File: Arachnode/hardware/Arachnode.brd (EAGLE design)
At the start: 71.1 x 33.7 mm, 37 parts, among them J1 PINHEAD-17-REV, J2 PINHEAD-17-REV, U1 BQ24210, U2 DS1337

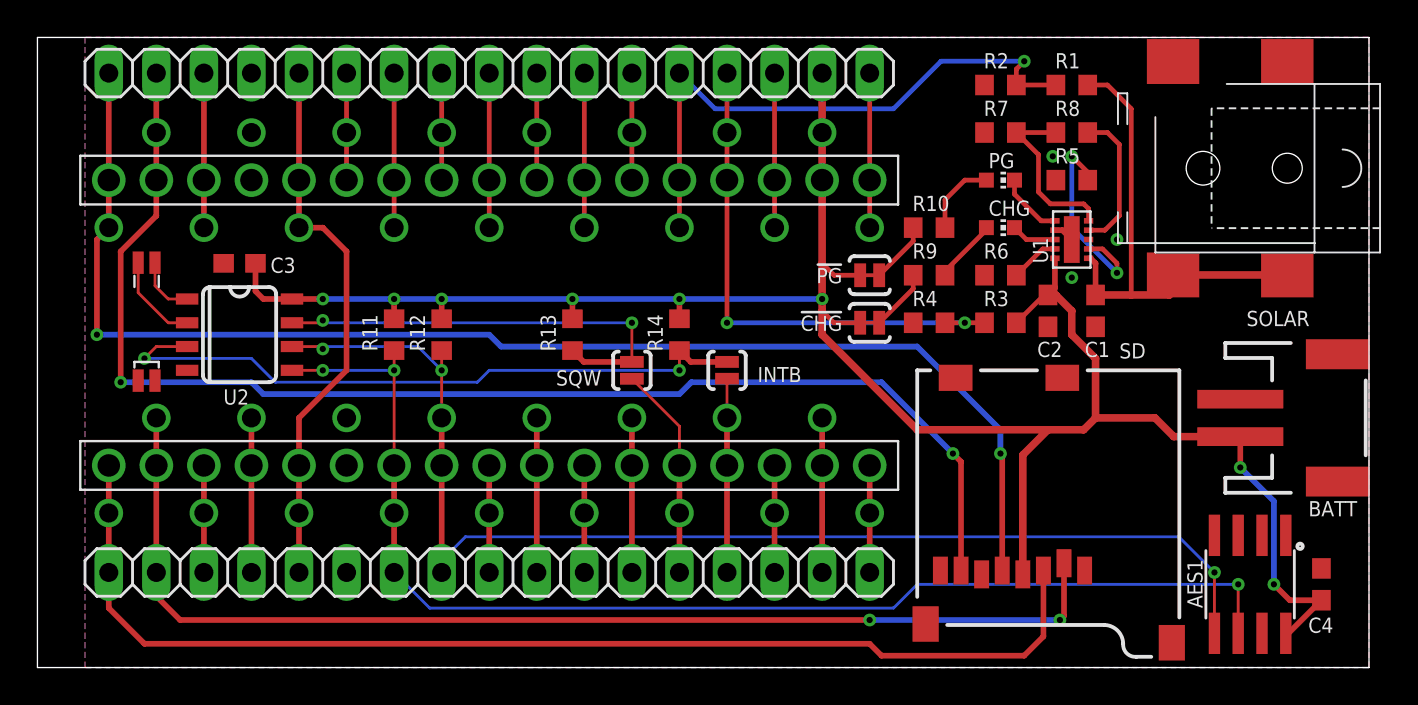
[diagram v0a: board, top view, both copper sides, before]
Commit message: -- Re-arranged Arachnode to solve connector interference. -- Created pinout diagrams for Arachnio -- Added sketch for serial console
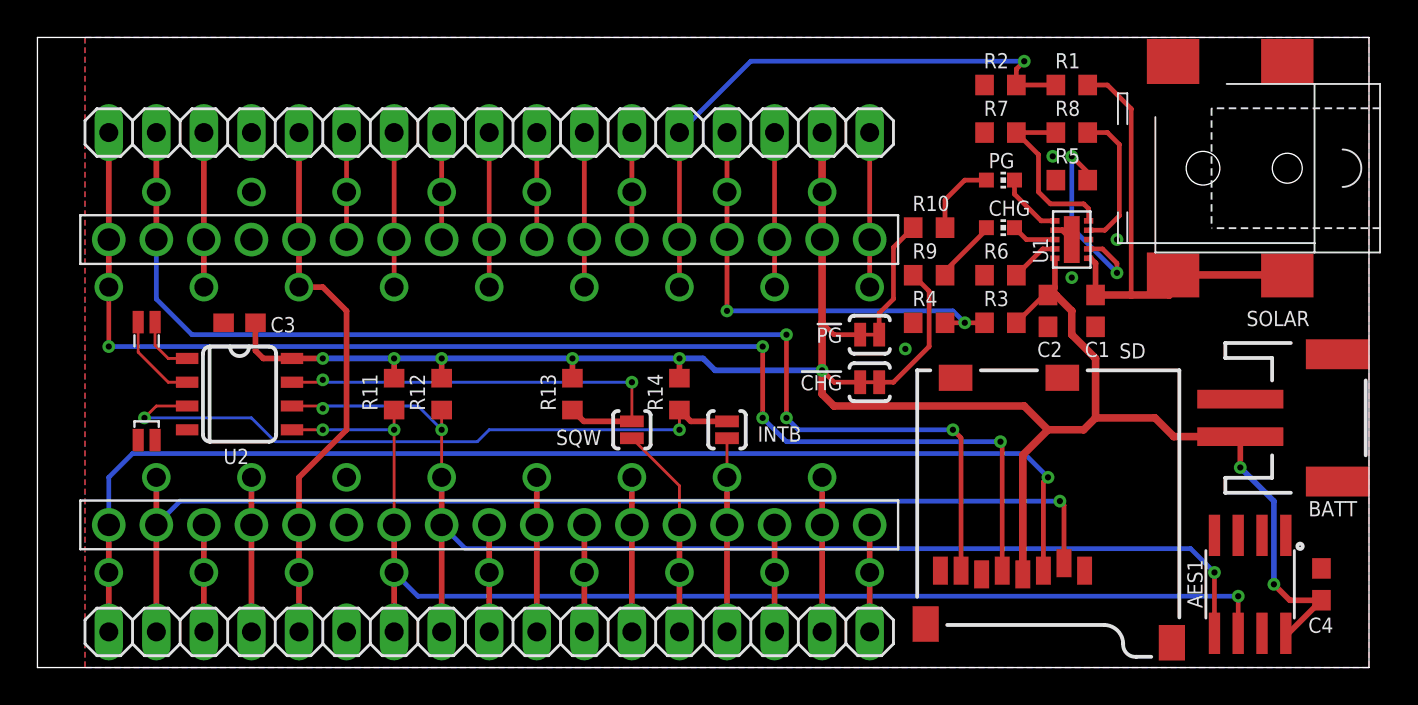
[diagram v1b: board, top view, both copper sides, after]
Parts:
- moved !CHG! 3.18 mm to (44.5, 12.1)
- moved !PG! 3.18 mm to (44.5, 14.6)
- moved J2 3.18 mm to (24.1, 19.7)
- moved JP2 3.18 mm to (24.1, 25.4)
- moved R11 3.18 mm to (19.1, 11.4)
- moved R12 3.18 mm to (21.6, 11.4)
- moved R13 3.18 mm to (28.6, 11.4)
- moved R14 3.18 mm to (34.3, 11.4)
- moved U2 3.18 mm to (10.8, 11.4)
- moved Y1 3.18 mm to (5.08, 15.9)
- moved J1 3.17 mm to (24.1, 4.45)
- moved JP1 3.17 mm to (24.1, -1.27)
- moved C3 3.17 mm to (10.8, 15.2)
- moved INTB 3.17 mm to (36.8, 9.53)
- moved SQW 3.17 mm to (31.8, 9.53)
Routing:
- net MISO: track 70.3 -> 64.6 mm, vias 2 -> 3
- net N$12: track 3.29 -> 7.62 mm
- net A0: track 28.1 -> 24.6 mm
- net N$13: track 3.29 -> 6.47 mm
- net MOSI: track 62.5 -> 64.6 mm, vias 0 -> 1
- net SCK: track 72.2 -> 70.3 mm, vias 2 -> 4
- net SDA: track 66.3 -> 64.9 mm
- net V_BATT: track 114.5 -> 113.5 mm
- net SS: track 61.4 -> 60.4 mm, vias 2 -> 1
- net SCL: track 67.0 -> 66.1 mm
- net GND: vias 3 -> 4

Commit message: ﻿-- added power switching to make USB power work correctly. # Please enter the commit message for your changes. Lines starting # with '#' will be ignored, and an empty message aborts the commit. # On branch arachnode-update # Your branch is up-to-date with 'origin/arachnode-update'. # # Changes to be committed: #	modified:   Arachnode/hardware/Arachnode.brd #	modified:   Arachnode/hardware/Arachnode.sch #
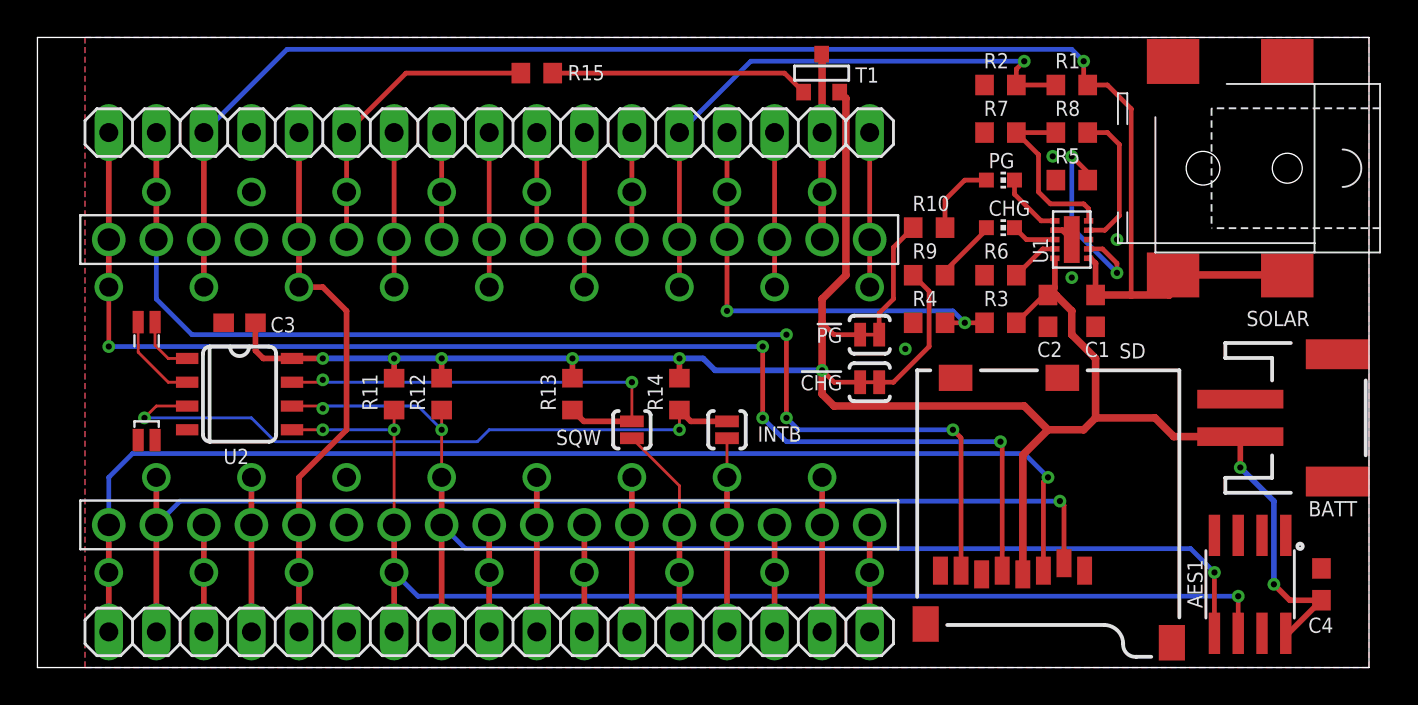
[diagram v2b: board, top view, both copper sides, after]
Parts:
- added R15: 4k7, resistor:R0603
- added T1: (no value), zetex:SOT-23
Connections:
- new net 3V3: J2.16, J2.33, JP2.16, T1.1
- net +5V: now also R15.2
- net N$1: now also R15.1, T1.3; no longer C1.2, R1.2, SOLAR.1A, SOLAR.1B, U1.1
- net VIN: now also C1.2, R1.2, SOLAR.1A, SOLAR.1B, U1.1
- net V_BATT: now also T1.2; no longer J2.16, J2.33, JP2.16
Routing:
- net VIN: track 8.25 -> 84.9 mm, vias 0 -> 1
- net N$1: track 26.1 -> 13.8 mm
- net +5V: track 5.71 -> 16.3 mm
- net 3V3: track 0.00 -> 9.92 mm
- net V_BATT: track 113.5 -> 116.3 mm
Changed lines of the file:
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@@
 <element name="U$1" library="SparkFun-Aesthetics" package="OSHW-LOGO-S" value="" x="60.325" y="13.97" smashed="yes" rot="MR0"/>
 <element name="U$2" library="logos-faves" package="LOGO-SM" value="" x="63.5" y="1.27" smashed="yes" rot="MR0"/>
+<element name="T1" library="zetex" package="SOT-23" value="" x="41.91" y="28.575" smashed="yes" rot="R180">
+<attribute name="OC_NEWARK" value="unknown" x="41.91" y="28.575" size="0.8128" layer="27" ratio="17" rot="R180" display="off"/>
+<attribute name="MPN" value="" x="41.91" y="28.575" size="0.8128" layer="27" ratio="17" rot="R180" display="off"/>
+<attribute name="MF" value="" x="41.91" y="28.575" size="0.8128" layer="27" ratio="17" rot="R180" display="off"/>
+<attribute name="OC_FARNELL" value="unknown" x="41.91" y="28.575" size="0.8128" layer="27" ratio="17" rot="R180" display="off"/>
+<attribute name="VALUE" x="43.307" y="26.797" size="1.27" layer="27" ratio="10" rot="R180"/>
+<attribute name="NAME" x="43.688" y="28.067" size="0.8128" layer="25" font="vector" ratio="17"/>
+</element>
+<element name="R15" library="resistor" package="R0603" value="4k7" x="26.67" y="28.575" smashed="yes" rot="R180">
+<attribute name="NAME" x="28.321" y="28.194" size="0.8128" layer="25" font="vector" ratio="17"/>
+</element>
 </elements>
 <signals>
@@
 <wire x1="16.51" y1="25.4" x2="16.51" y2="22.225" width="0.254" layer="1"/>
 <wire x1="16.51" y1="22.225" x2="16.51" y2="19.685" width="0.254" layer="1"/>
+<contactref element="R15" pad="2"/>
+<wire x1="25.82" y1="28.575" x2="19.685" y2="28.575" width="0.254" layer="1"/>
+<wire x1="19.685" y1="28.575" x2="16.51" y2="25.4" width="0.254" layer="1"/>
 </signal>
 <signal name="VIN">
@@
 <wire x1="8.89" y1="17.145" x2="8.89" y2="19.685" width="0.3048" layer="1"/>
 <wire x1="8.89" y1="19.685" x2="8.89" y2="25.4" width="0.3048" layer="1"/>
+<contactref element="SOLAR" pad="1A"/>
+<contactref element="SOLAR" pad="1B"/>
+<contactref element="R1" pad="2"/>
+<contactref element="U1" pad="1"/>
+<contactref element="C1" pad="2"/>
+<wire x1="56.145" y1="18.685" x2="56.245" y2="18.685" width="0.3048" layer="1"/>
+<wire x1="56.245" y1="18.685" x2="56.515" y2="18.415" width="0.3048" layer="1"/>
+<wire x1="56.515" y1="18.415" x2="56.515" y2="16.725" width="0.3048" layer="1"/>
+<wire x1="56.515" y1="16.725" x2="58.42" y2="16.725" width="0.4064" layer="1"/>
+<wire x1="58.42" y1="16.725" x2="60.455" y2="16.725" width="0.4064" layer="1"/>
+<wire x1="60.455" y1="16.725" x2="60.655" y2="17.795" width="0.4064" layer="1"/>
+<wire x1="60.655" y1="17.795" x2="66.755" y2="17.795" width="0.4064" layer="1"/>
+<wire x1="56.095" y1="27.94" x2="57.15" y2="27.94" width="0.254" layer="1"/>
+<wire x1="57.15" y1="27.94" x2="58.42" y2="26.67" width="0.254" layer="1"/>
+<wire x1="58.42" y1="26.67" x2="58.42" y2="16.725" width="0.254" layer="1"/>
+<wire x1="56.095" y1="27.94" x2="55.88" y2="27.94" width="0.254" layer="1"/>
+<wire x1="55.88" y1="27.94" x2="55.88" y2="29.21" width="0.254" layer="1"/>
+<via x="55.88" y="29.21" extent="1-16" drill="0.3302"/>
+<wire x1="55.88" y1="29.21" x2="55.245" y2="29.845" width="0.254" layer="16"/>
+<wire x1="55.245" y1="29.845" x2="13.335" y2="29.845" width="0.254" layer="16"/>
+<wire x1="13.335" y1="29.845" x2="8.89" y2="25.4" width="0.254" layer="16"/>
 </signal>
 <signal name="MISO">
@@
 <contactref element="BATT" pad="2"/>
 <contactref element="SD" pad="4"/>
-<contactref element="J2" pad="16"/>
-<contactref element="J2" pad="33"/>
-<contactref element="JP2" pad="16"/>
 <contactref element="R3" pad="2"/>
 <contactref element="U1" pad="10"/>
@@
 <wire x1="52.63" y1="1.8" x2="52.63" y2="8.18" width="0.4064" layer="1"/>
 <wire x1="52.63" y1="8.18" x2="53.975" y2="9.525" width="0.4064" layer="1"/>
-<wire x1="41.91" y1="25.4" x2="41.91" y2="22.225" width="0.4064" layer="1"/>
-<wire x1="41.91" y1="22.225" x2="41.91" y2="19.685" width="0.4064" layer="1"/>
-<wire x1="41.91" y1="19.685" x2="41.91" y2="15.24" width="0.4064" layer="1"/>
 <wire x1="41.91" y1="15.24" x2="41.91" y2="12.7" width="0.4064" layer="1"/>
 <wire x1="41.91" y1="12.7" x2="41.91" y2="11.43" width="0.4064" layer="1"/>
@@
 <wire x1="66.04" y1="5.715" x2="64.245" y2="7.51" width="0.3048" layer="16"/>
 <wire x1="66.89" y1="0.42" x2="66.04" y2="1.27" width="0.3048" layer="1"/>
-</signal>
-<signal name="N$1">
-<contactref element="SOLAR" pad="1A"/>
-<contactref element="SOLAR" pad="1B"/>
-<contactref element="R1" pad="2"/>
-<contactref element="U1" pad="1"/>
-<contactref element="C1" pad="2"/>
-<wire x1="56.145" y1="18.685" x2="56.245" y2="18.685" width="0.3048" layer="1"/>
-<wire x1="56.245" y1="18.685" x2="56.515" y2="18.415" width="0.3048" layer="1"/>
-<wire x1="56.515" y1="18.415" x2="56.515" y2="16.725" width="0.3048" layer="1"/>
-<wire x1="56.515" y1="16.725" x2="58.42" y2="16.725" width="0.4064" layer="1"/>
-<wire x1="58.42" y1="16.725" x2="60.455" y2="16.725" width="0.4064" layer="1"/>
-<wire x1="60.455" y1="16.725" x2="60.655" y2="17.795" width="0.4064" layer="1"/>
-<wire x1="60.655" y1="17.795" x2="66.755" y2="17.795" width="0.4064" layer="1"/>
-<wire x1="56.095" y1="27.94" x2="57.15" y2="27.94" width="0.254" layer="1"/>
-<wire x1="57.15" y1="27.94" x2="58.42" y2="26.67" width="0.254" layer="1"/>
-<wire x1="58.42" y1="26.67" x2="58.42" y2="16.725" width="0.254" layer="1"/>
+<contactref element="T1" pad="2"/>
+<wire x1="41.91" y1="15.24" x2="41.91" y2="16.51" width="0.4064" layer="1"/>
+<wire x1="41.91" y1="16.51" x2="43.18" y2="17.78" width="0.4064" layer="1"/>
+<wire x1="43.18" y1="17.78" x2="43.18" y2="27.2288" width="0.4064" layer="1"/>
+<wire x1="43.18" y1="27.2288" x2="42.8498" y2="27.559" width="0.4064" layer="1"/>
 </signal>
 <signal name="IO12">
@@
 <wire x1="34.29" y1="9.525" x2="34.29" y2="10.58" width="0.1524" layer="1"/>
 </signal>
+<signal name="N$1">
+<contactref element="R15" pad="1"/>
+<contactref element="T1" pad="3"/>
+<wire x1="27.52" y1="28.575" x2="39.9034" y2="28.575" width="0.254" layer="1"/>
+<wire x1="39.9034" y1="28.575" x2="40.9194" y2="27.559" width="0.254" layer="1"/>
+</signal>
+<signal name="3V3">
+<contactref element="J2" pad="16"/>
+<contactref element="J2" pad="33"/>
+<contactref element="JP2" pad="16"/>
+<wire x1="41.91" y1="25.4" x2="41.91" y2="22.225" width="0.4064" layer="1"/>
+<wire x1="41.91" y1="22.225" x2="41.91" y2="19.685" width="0.4064" layer="1"/>
+<contactref element="T1" pad="1"/>
+<wire x1="41.91" y1="25.4" x2="41.91" y2="29.5656" width="0.4064" layer="1"/>
+<wire x1="41.91" y1="29.5656" x2="41.8846" y2="29.591" width="0.4064" layer="1"/>
+</signal>
 </signals>

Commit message: Moved the Arachnode connectors around for USB clearance.
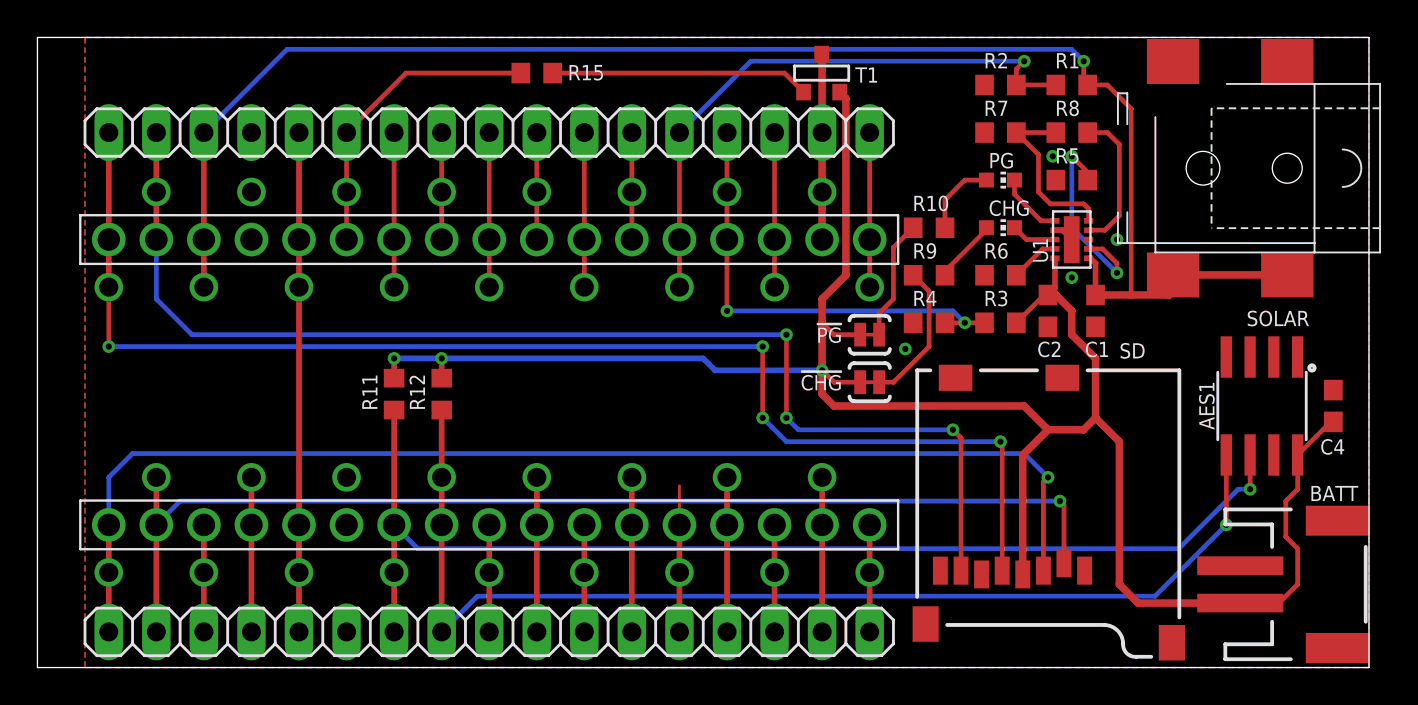
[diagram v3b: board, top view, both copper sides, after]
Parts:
- removed C3: 100n, resistor:C0603
- removed INTB, SQW: (no value), SparkFun-Passives:PAD-JUMPER-2-NO_YES_SILK
- removed R13, R14: 4k7, resistor:R0603
- removed U2: DS1337, SparkFun-FreqCtrl:SO08-TIGHT
- removed Y1: (no value), SparkFun-FreqCtrl:CRYSTAL-32KHZ-SMD_EPSON_MC146
- moved AES1 9.55 mm to (65.4, 10.8)
- moved C4 9.55 mm to (69.2, 10.8)
- moved BATT 8.89 mm to (67.9, 1.27)
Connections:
- removed net N$14: U2.2, Y1.P$1
- removed net N$15: INTB.2, R14.1, U2.3
- removed net N$2: R13.1, SQW.2, U2.7
- removed net N$4: U2.1, Y1.P$2
- net GND: no longer C3.2, U2.4
- net IO8: no longer SQW.1
- net IO9: no longer INTB.1
- net SCL: no longer U2.6
- net SDA: no longer U2.5
- net V_BATT: no longer C3.1, R13.2, R14.2, U2.8
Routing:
- net N$15: track 35.8 -> 0.00 mm, vias 2 -> 0
- net N$2: track 23.8 -> 0.00 mm, vias 2 -> 0
- net SCL: track 66.1 -> 59.9 mm, vias 3 -> 1
- net N$14: track 4.88 -> 0.00 mm
- net SDA: track 64.9 -> 61.2 mm, vias 3 -> 1
- net V_BATT: track 116.3 -> 112.7 mm, vias 8 -> 3
- net IO8: track 11.4 -> 7.80 mm
- net N$4: track 3.24 -> 0.00 mm
- net RESET: track 29.5 -> 26.7 mm
- net IO9: track 10.3 -> 8.25 mm
